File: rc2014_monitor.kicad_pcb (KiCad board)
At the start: 2 copper layers, 101.6 x 50.8 mm, 60 parts, among them J1 Z80 Bus, J2 Pro Bus, J3 USB_B_Micro, J4 M3 Mounting Hole, SW1 Line Selection, SW2 SW_Push, SW3 SW_Push, SW4 Run/Step Mode, U1 74HCT541, U11 74HCT00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

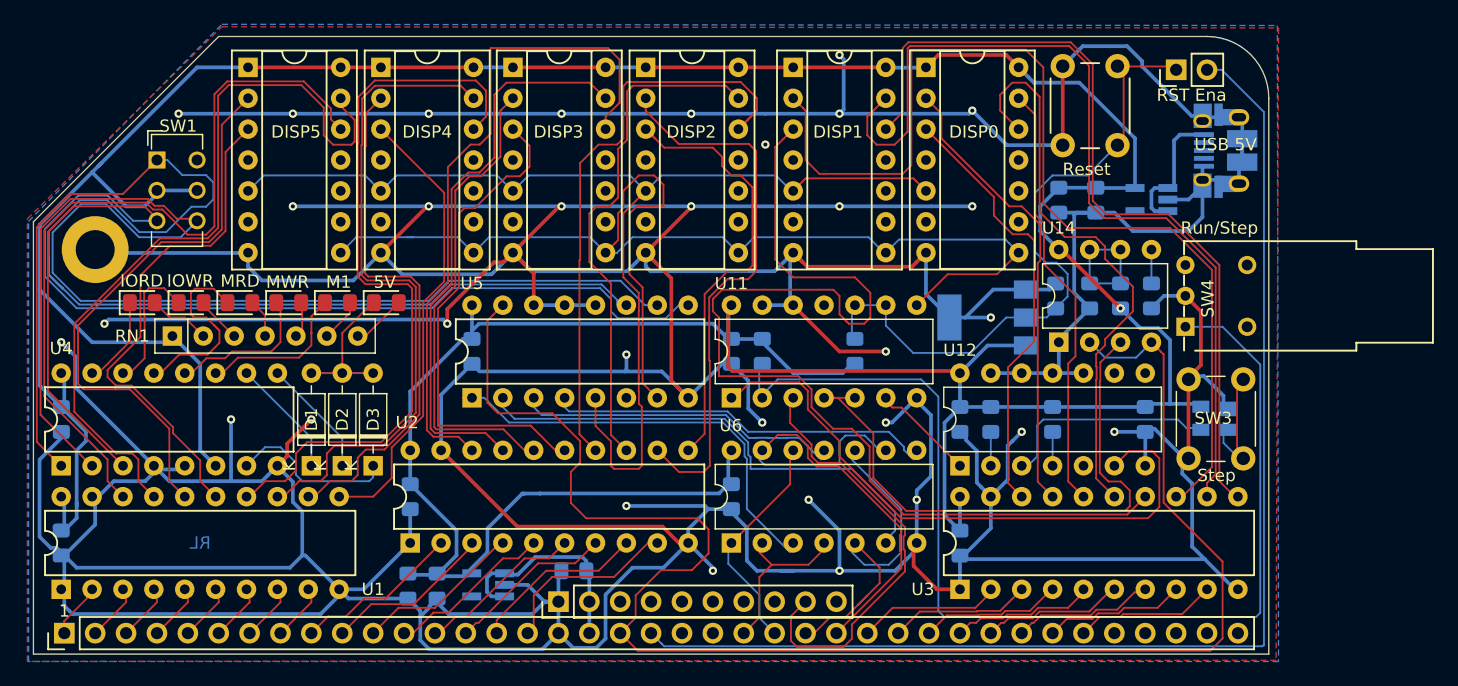
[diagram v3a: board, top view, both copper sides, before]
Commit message: removed rotary, rerouted
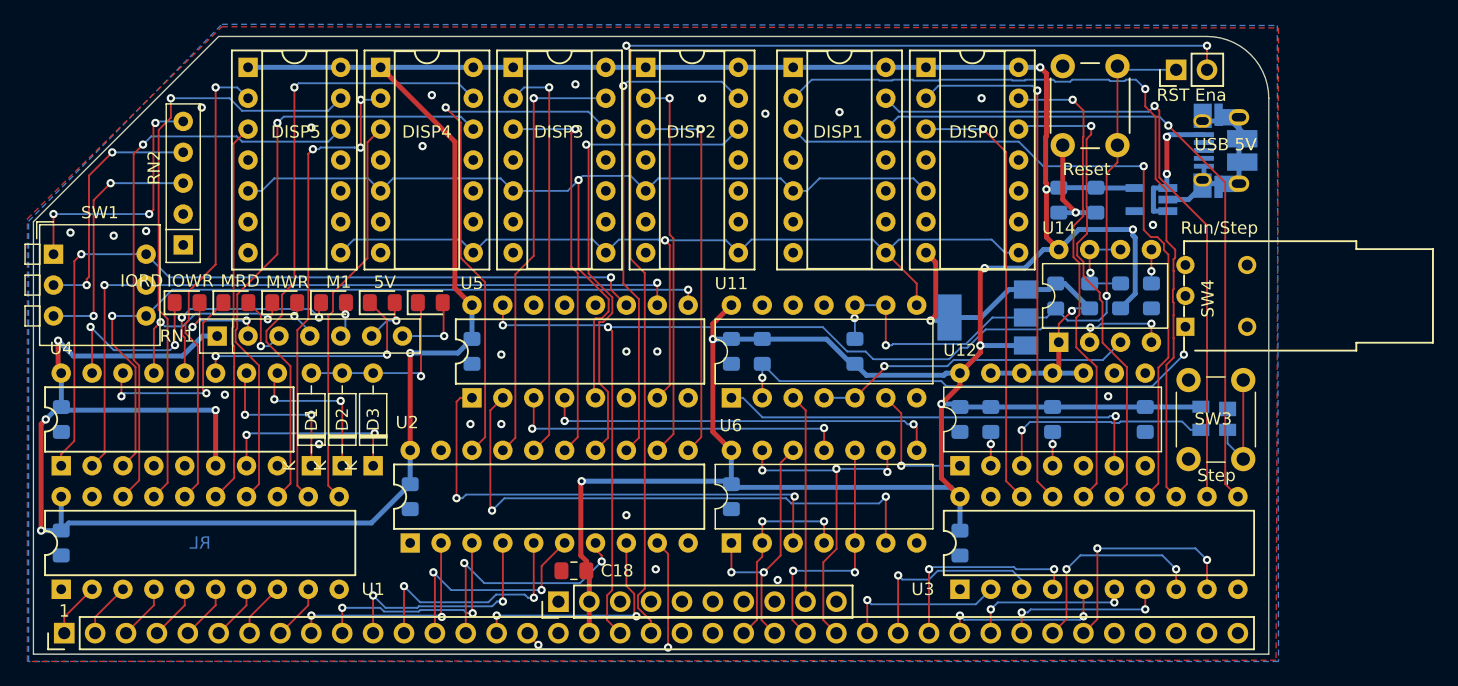
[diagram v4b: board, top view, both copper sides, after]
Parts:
- removed C10: 100nF, Capacitor_SMD:C_0805_2012Metric_Pad1.15x1.40mm_HandSolder
- removed C8: 1uF, Capacitor_SMD:C_0805_2012Metric_Pad1.15x1.40mm_HandSolder
- removed J4: M3 Mounting Hole, MountingHole:MountingHole_3.2mm_M3_ISO14580_Pad
- removed U8: MAX40200AUK, Package_TO_SOT_SMD:SOT-23-5_HandSoldering
- added G***: LOGO, Logos:asian_tiger, F.Cu at (129.2, 100.2)
- added RN2: 1K, Resistor_THT:R_Array_SIP5, F.Cu at (87.8, 93.9)
- C18: moved to F.Cu
- SW1: value Line Selection -> SW_DIP_x03; footprint Button_Switch_THT:SW_Greyhill_94HBB08RAT_Octal_Angled -> Button_Switch_THT:SW_DIP_SPSTx03_Piano_CTS_Series194-3MSTN_W7.62mm_P2.54mm
- moved SW1 11.1 mm to (77.1, 94.6)
- moved LED4 3.68 mm to (100.1, 98.6)
- moved LED5 3.68 mm to (104.1, 98.6)
- moved RN1 3.68 mm to (90.6, 101.3)
- moved LED1 3.68 mm to (88.1, 98.6)
- moved LED2 3.68 mm to (92.1, 98.6)
- moved LED3 3.68 mm to (96.1, 98.6)
- moved LED6 3.62 mm to (108.1, 98.6)
- moved SW3 0.06 mm to (170.4, 111.5)
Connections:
- net Net-(SW1-Pad4) renamed /LatchSelector/C
- C1 pad 1: +5V -> 5V
- C11 pad 1: +5V -> 5V
- C12 pad 1: +5V -> 5V
- C13 pad 1: +5V -> 5V
- C17 pad 1: +5V -> 5V
- C2 pad 1: +5V -> 5V
- C3 pad 1: +5V -> 5V
- C4 pad 1: +5V -> 5V
- C5 pad 1: +5V -> 5V
- C6 pad 1: +5V -> 5V
- C7 pad 1: +5V -> 5V
- DISP0 pad 1: +5V -> 5V
- DISP0 pad 14: +5V -> 5V
- DISP1 pad 1: +5V -> 5V
- DISP1 pad 14: +5V -> 5V
- DISP2 pad 1: +5V -> 5V
- DISP2 pad 14: +5V -> 5V
- DISP3 pad 1: +5V -> 5V
- DISP3 pad 14: +5V -> 5V
- DISP4 pad 1: +5V -> 5V
- DISP4 pad 14: +5V -> 5V
- DISP5 pad 1: +5V -> 5V
- DISP5 pad 14: +5V -> 5V
- R1 pad 1: +5V -> 5V
- R2 pad 1: +5V -> 5V
- R3 pad 2: +5V -> 5V
- R4 pad 2: +5V -> 5V
- R5 pad 2: +5V -> 5V
- RN1 pad 1: +5V -> 5V
- SW1 pad 1: Net-(SW1-Pad1) -> Net-(RN2-Pad5)
- SW1 pad 2: Net-(SW1-Pad2) -> Net-(RN2-Pad4)
- U1 pad 20: +5V -> 5V
- U11 pad 14: +5V -> 5V
- U12 pad 14: +5V -> 5V
- U13 pad 4: +5V -> 5V
- U14 pad 8: +5V -> 5V
- U2 pad 20: +5V -> 5V
- U3 pad 20: +5V -> 5V
- U4 pad 1: Net-(SW1-Pad1) -> /LatchSelector/A
- U4 pad 16: +5V -> 5V
- U4 pad 2: Net-(SW1-Pad2) -> /LatchSelector/B
- U4 pad 6: +5V -> 5V
- U5 pad 10: Net-(SW1-Pad2) -> /LatchSelector/B
- U5 pad 11: Net-(SW1-Pad1) -> /LatchSelector/A
- U5 pad 16: +5V -> 5V
- U6 pad 14: +5V -> 5V
- U7 pad 5: +5V -> 5V
- U9 pad 3: +5V -> 5V
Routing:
- net GND: track 808.2 -> 59.9 mm, vias 32 -> 27
- net +5V: track 368.4 -> 0.00 mm, vias 1 -> 0
- net 5V: track 17.9 -> 361.2 mm, vias 0 -> 13
- net Net-(SW1-Pad1): track 113.1 -> 0.00 mm
- net Net-(SW1-Pad2): track 105.6 -> 0.00 mm
- net /LatchSelector/A: track 0.00 -> 65.2 mm, vias 0 -> 2
- net /LatchSelector/B: track 0.00 -> 62.7 mm, vias 0 -> 2
- net Net-(R3-Pad1): track 91.1 -> 41.5 mm, vias 0 -> 2
- net ~M1: track 131.6 -> 86.0 mm, vias 0 -> 4
- net /LatchSelector/C: track 103.8 -> 63.1 mm, vias 0 -> 2
- net D_D4: track 87.5 -> 59.2 mm, vias 0 -> 1
- net Net-(U11-Pad4): track 49.7 -> 26.4 mm, vias 0 -> 1
- net RST: track 102.3 -> 79.1 mm, vias 0 -> 1
- net Net-(RN2-Pad5): track 0.00 -> 21.2 mm, vias 0 -> 3
- net Net-(RN2-Pad3): track 0.00 -> 20.8 mm, vias 0 -> 2
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
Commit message: added dip sw for latch selection
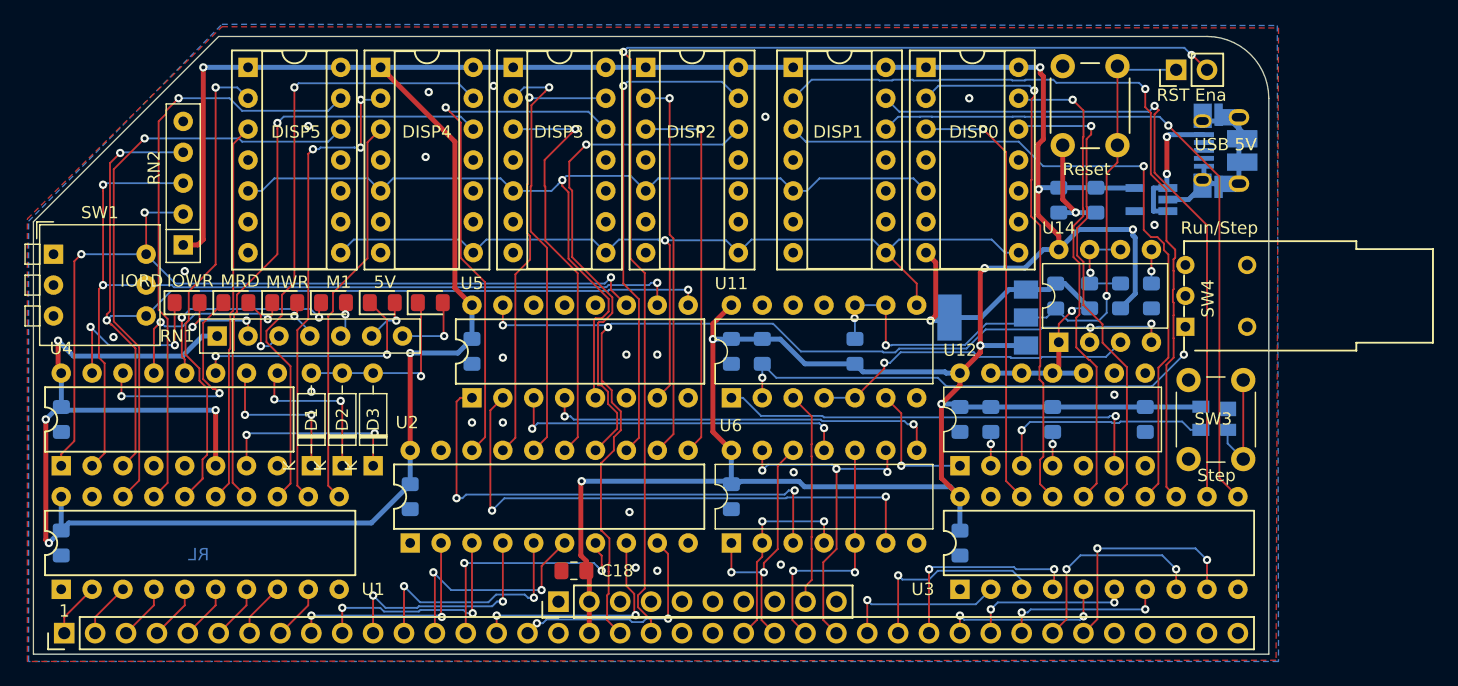
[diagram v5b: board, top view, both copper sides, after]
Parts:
- removed G***: LOGO, Logos:asian_tiger
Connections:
- RN2 pad 1: GND -> 5V
- RN2 pad 2: (no net) -> /LatchSelector/A
- RN2 pad 3: Net-(RN2-Pad3) -> /LatchSelector/B
- RN2 pad 4: Net-(RN2-Pad4) -> /LatchSelector/C
- RN2 pad 5: Net-(RN2-Pad5) -> (no net)
- SW1 pad 1: Net-(RN2-Pad5) -> GND
- SW1 pad 2: Net-(RN2-Pad4) -> GND
- SW1 pad 3: Net-(RN2-Pad3) -> GND
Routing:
- net 5V: track 361.2 -> 383.0 mm, vias 13 -> 14
- net Net-(RN2-Pad5): track 21.2 -> 0.00 mm, vias 3 -> 0
- net Net-(RN2-Pad3): track 20.8 -> 0.00 mm, vias 2 -> 0
- net Net-(RN2-Pad4): track 20.4 -> 0.00 mm, vias 2 -> 0
- net /LatchSelector/C: track 63.1 -> 83.0 mm, vias 2 -> 3
- net /LatchSelector/B: track 62.7 -> 78.2 mm, vias 2 -> 3
- net /LatchSelector/A: track 65.2 -> 72.4 mm, vias 2 -> 3
- net A0: track 21.1 -> 18.8 mm
- net D_A3: track 40.4 -> 42.5 mm
- net D_A4: track 32.3 -> 34.2 mm
- net Net-(LED2-Pad1): track 17.1 -> 18.8 mm
- net ~M1: track 86.0 -> 87.5 mm
- net D_A15: track 47.2 -> 48.6 mm
- net ~RESET: track 99.3 -> 98.1 mm
- net D_A5: track 33.7 -> 34.8 mm
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
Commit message: tightened up gnd plane and schematics
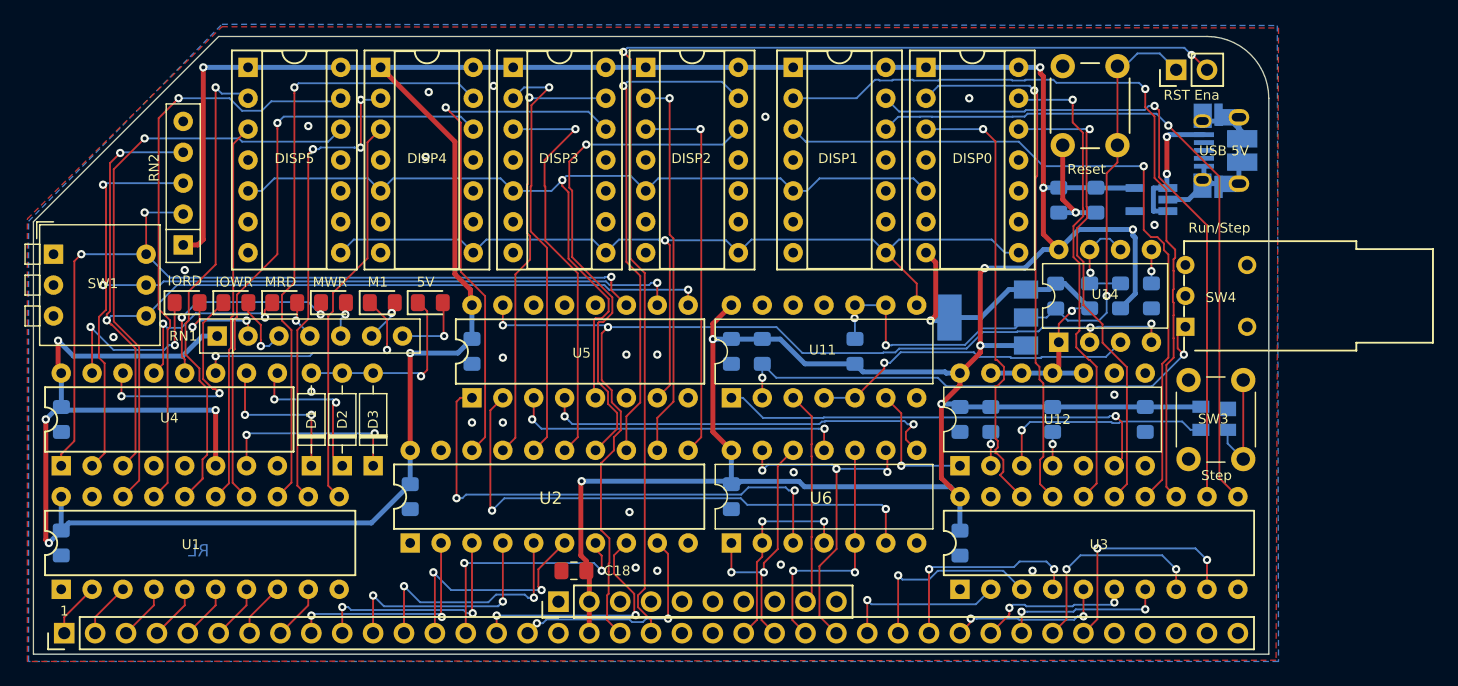
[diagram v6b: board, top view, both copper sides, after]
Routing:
- net D_D0: track 36.2 -> 37.4 mm
- net Net-(D2-Pad1): track 12.8 -> 11.6 mm
- net ~RST: track 53.2 -> 54.3 mm
- net D_A10: track 51.2 -> 50.2 mm
- net D3: track 14.1 -> 13.2 mm
- net A1: track 19.1 -> 20.0 mm
- net 5V: track 383.0 -> 382.2 mm
- net IO_WR: track 28.8 -> 28.0 mm
- net Net-(C15-Pad1): track 7.92 -> 8.65 mm
- net IO_RD: track 32.7 -> 33.5 mm
- net D4: track 13.4 -> 12.7 mm
- net M_RD: track 46.4 -> 45.7 mm
- net Net-(LED4-Pad2): track 2.39 -> 2.92 mm
- net D_A13: track 39.2 -> 38.7 mm
- net /LatchSelector/A: track 72.4 -> 71.9 mm
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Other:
- board text added: "RC2014 Bus Monitor 1.0 by Hyiger Designs"
- board text removed: "RC2014 Bus Monitor 0.3 by Hyiger Designs"

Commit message: extended active high reset to displays and ics
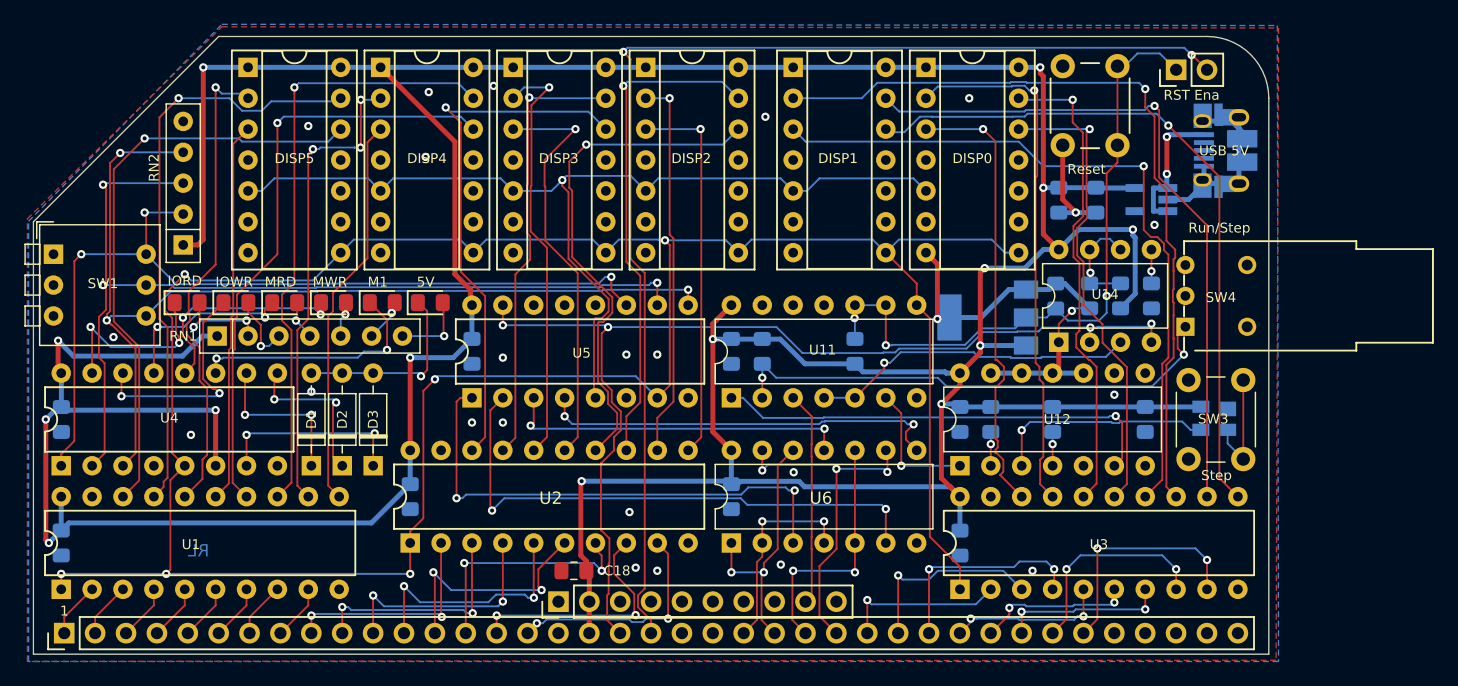
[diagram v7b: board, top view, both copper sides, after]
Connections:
- U1 pad 1: GND -> RST
- U2 pad 1: GND -> RST
- U3 pad 1: GND -> RST
- U4 pad 5: GND -> RST
- U5 pad 10: /LatchSelector/B -> (no net)
- U5 pad 11: /LatchSelector/A -> (no net)
- U5 pad 9: /LatchSelector/C -> (no net)
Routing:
- net RST: track 79.1 -> 210.5 mm, vias 1 -> 6
- net GND: track 59.9 -> 59.1 mm

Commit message: fixed via sizes and silk
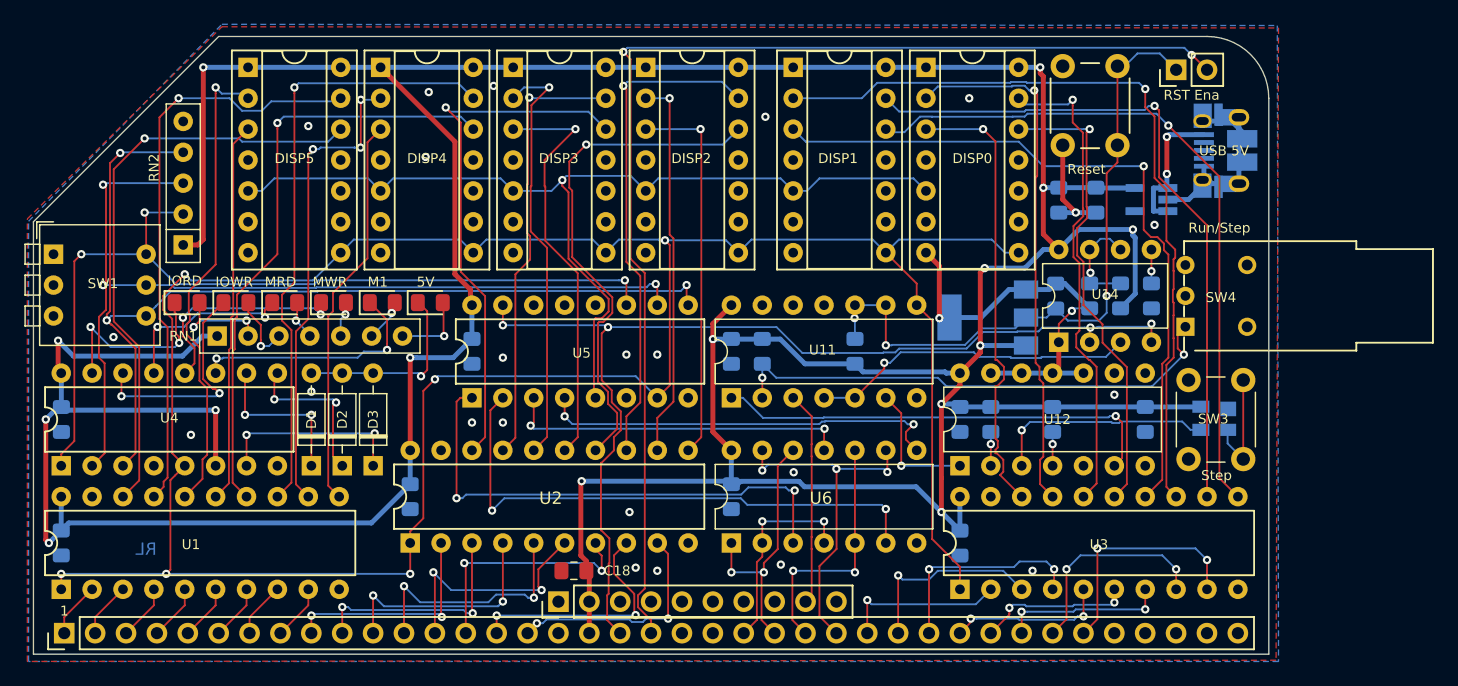
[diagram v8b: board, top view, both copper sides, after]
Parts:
- added G***: LOGO, Logos:asian_tiger, F.Cu at (125.9, 89.2)
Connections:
- U5 pad 10: (no net) -> /LatchSelector/B
- U5 pad 11: (no net) -> /LatchSelector/A
- U5 pad 9: (no net) -> /LatchSelector/C
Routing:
- net 5V: track 382.0 -> 383.8 mm, vias 14 -> 15
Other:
- board text added: "RC2014 Bus Monitor 2.0 by Hyiger Designs"
- board text removed: "RC2014 Bus Monitor 1.0 by Hyiger Designs"
